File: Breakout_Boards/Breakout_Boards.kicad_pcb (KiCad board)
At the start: 2 copper layers, 3 parts, among them J1 2xRJ_45, J2 Conn_01x06_Pin, J3 Conn_01x06_Pin

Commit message: Active Electrode
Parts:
- J1: value 2xRJ_45 -> Conn_01x06_Pin; footprint TE_2xRJ45:TE_2xRJ45 -> Connector_PinSocket_2.54mm:PinSocket_1x06_P2.54mm_Vertical
- J2: value Conn_01x06_Pin -> 2xRJ_45; footprint Connector_PinSocket_2.54mm:PinSocket_1x06_P2.54mm_Vertical -> TE_2xRJ45:TE_2xRJ45
- moved J2 31.2 mm to (16.0, 10.4), turned to 180 degrees
- moved J1 24.9 mm to (21.1, 35.6)
- moved J3 13.4 mm to (7.11, 35.5), turned to 180 degrees
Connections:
- J3 pad 2: /Blue_2 -> /Ethernet_Breakout/Blue_2
- J3 pad 3: /Blue_White_2 -> /Ethernet_Breakout/Blue_White_2
- J3 pad 4: /Green_2 -> /Ethernet_Breakout/Green_2
- J3 pad 5: /Green_White_2 -> /Ethernet_Breakout/Green_White_2
- J3 pad 6: /Orange_2 -> /Ethernet_Breakout/Orange_2
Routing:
- net /Blue_White_2: track 48.1 -> 0.00 mm
- net /Blue_White: track 36.0 -> 0.00 mm
- net /Green_White_2: track 34.3 -> 0.00 mm
- net /Green_White: track 32.0 -> 0.00 mm
- net /Ethernet_Breakout/Blue_White: track 0.00 -> 31.5 mm
- net /Ethernet_Breakout/Blue_White_2: track 0.00 -> 31.1 mm
- net /Ethernet_Breakout/Green_White: track 0.00 -> 21.1 mm
- net /Ethernet_Breakout/Green_White_2: track 0.00 -> 20.3 mm
- net /Ethernet_Breakout/Blue_2: track 0.00 -> 17.3 mm
- net /Ethernet_Breakout/Blue: track 0.00 -> 17.1 mm
- net /Orange_2: track 13.9 -> 0.00 mm
- net /Blue: track 13.0 -> 0.00 mm
- net /Green_2: track 12.9 -> 0.00 mm
- net /Green: track 12.0 -> 0.00 mm
- net /Blue_2: track 11.8 -> 0.00 mm
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
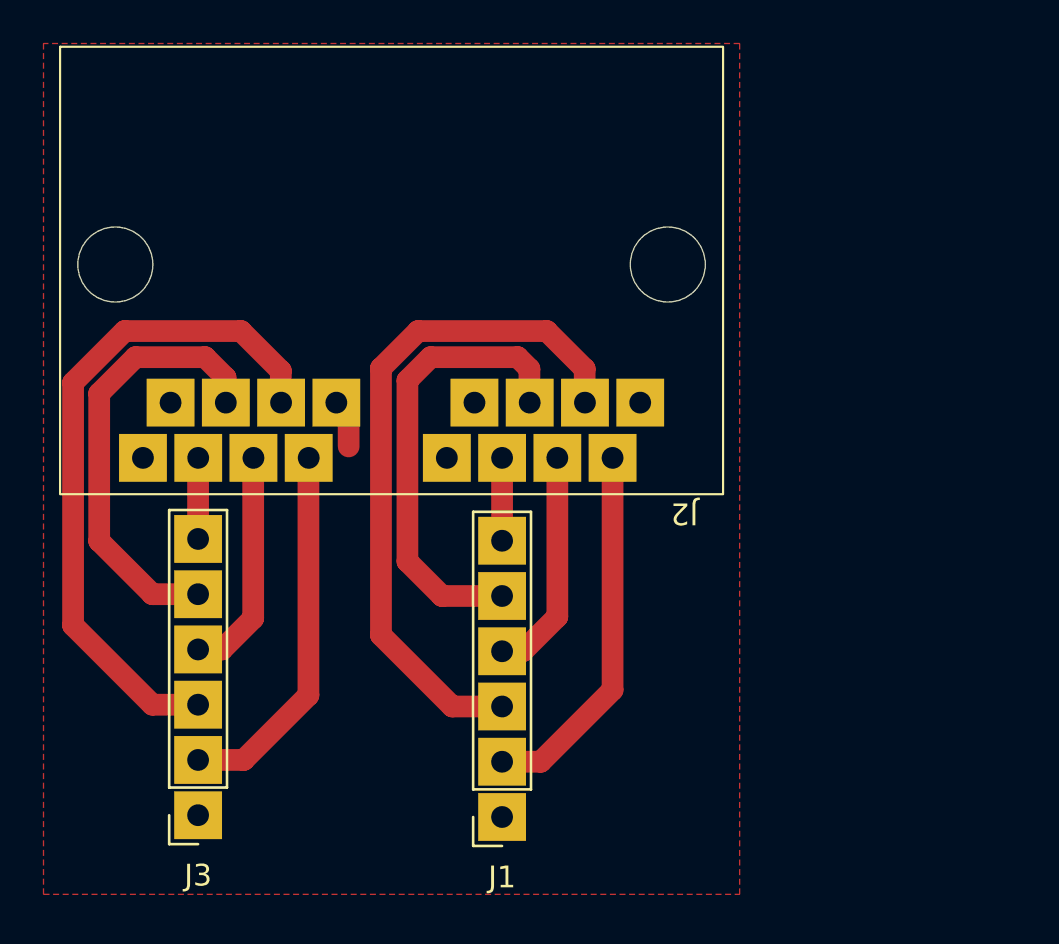
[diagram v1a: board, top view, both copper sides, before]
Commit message: Mill Digital Select breakout board and more active electrodes
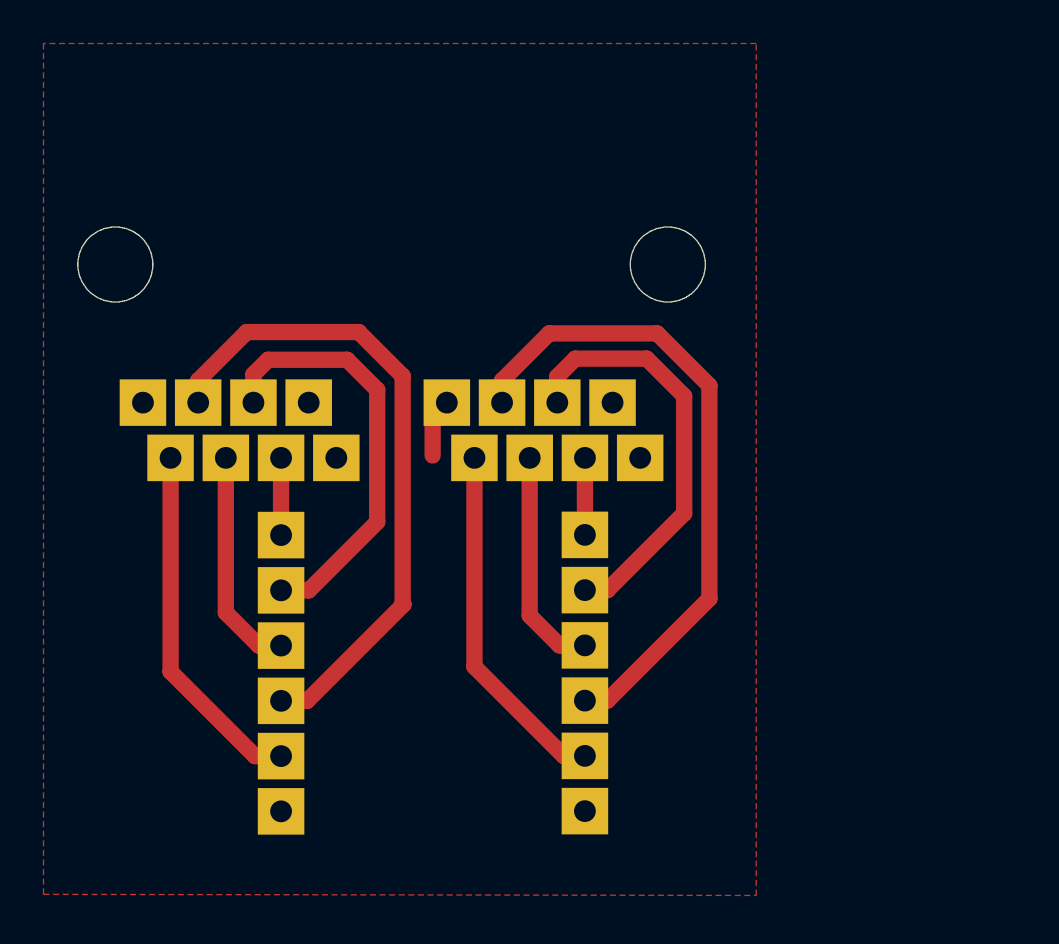
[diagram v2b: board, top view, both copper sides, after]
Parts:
- J1, J2, J3: moved to B.Cu
- moved J3 17.8 mm to (24.9, 35.3), turned to 0 degrees
- moved J1 10.2 mm to (10.9, 35.3), turned to 0 degrees
- turned J2 to 0 degrees
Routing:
- net /Ethernet_Breakout/Green_White: track 21.1 -> 19.6 mm
- net /Ethernet_Breakout/Blue_White: track 31.5 -> 30.2 mm
- net /Ethernet_Breakout/Blue_White_2: track 31.1 -> 29.9 mm
- net GND: track 1.52 -> 2.70 mm
- net /Ethernet_Breakout/Blue_2: track 17.3 -> 16.4 mm
- net /Ethernet_Breakout/Green_White_2: track 20.3 -> 19.5 mm
- net /Ethernet_Breakout/Blue: track 17.1 -> 16.5 mm
